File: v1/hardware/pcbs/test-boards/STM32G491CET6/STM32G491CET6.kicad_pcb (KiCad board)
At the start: 2 copper layers, 43 x 38 mm, 43 parts, among them J1 Conn_02x10_Odd_Even, J2 Conn_02x10_Odd_Even, J3 Conn_01x04, U1 STM32G491CETx, Y1 Crystal_GND24, Y2 Crystal

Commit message: not sure what i did
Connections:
- C6 pad 2: Net-(U1-VBAT) -> +3V3
- U1 pad 1: Net-(U1-VBAT) -> +3V3
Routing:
- net +3V3: track 35.4 -> 39.0 mm
- net Net-(U1-VBAT): track 3.65 -> 0.00 mm

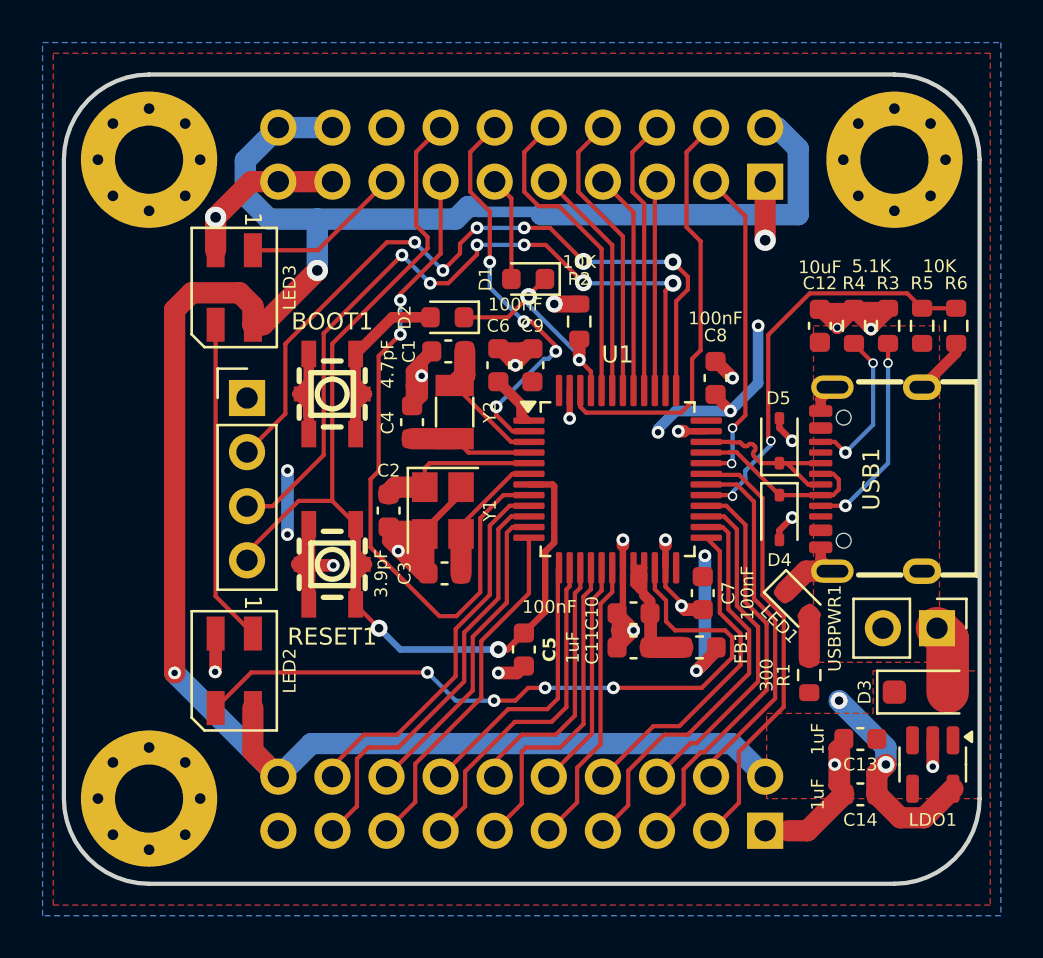
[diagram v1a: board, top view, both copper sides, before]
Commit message: fixed STM32G4 breakout board boot pin floating, and changed RGB LEDs to indicator LED
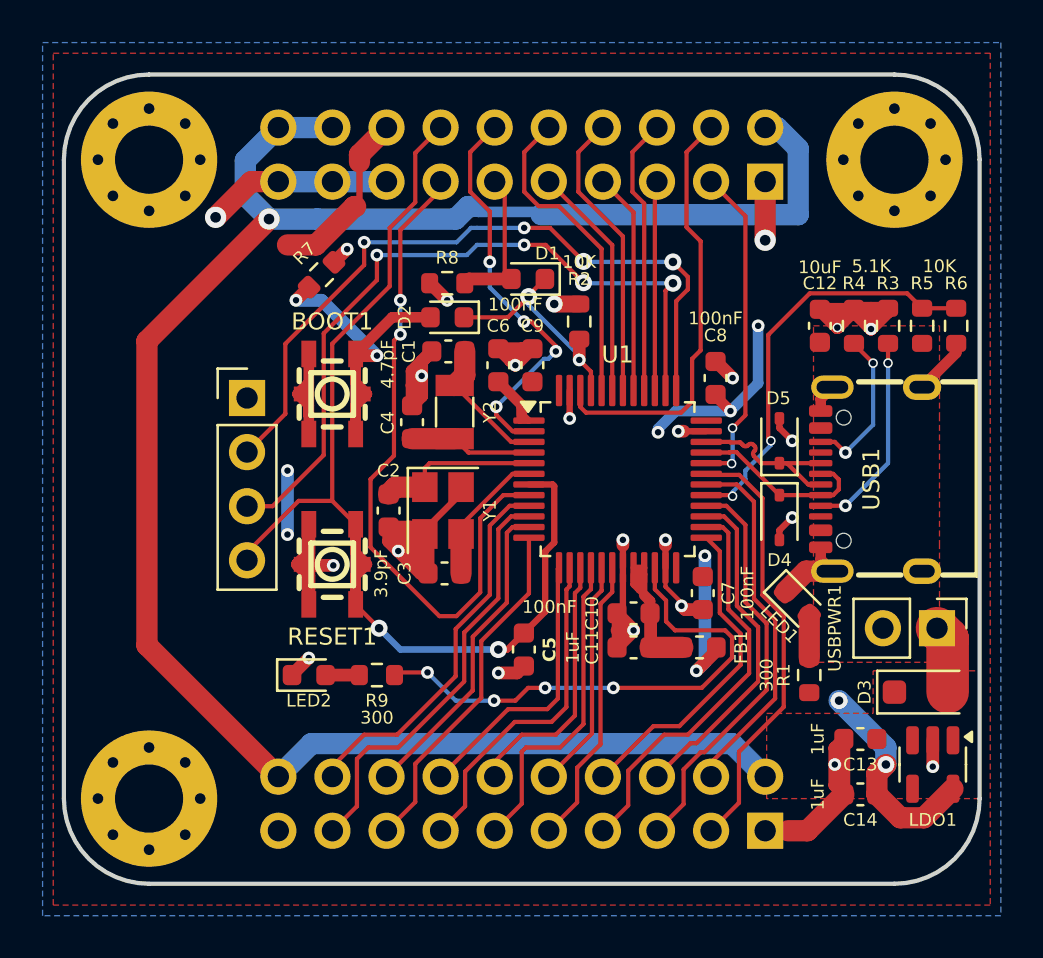
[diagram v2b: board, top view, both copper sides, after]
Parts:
- removed LED3: SK6812MINI, LED_SMD:LED_SK6812MINI_PLCC4_3.5x3.5mm_P1.75mm
- added R7: 10K, Resistor_SMD:R_0603_1608Metric, F.Cu at (-9.40, -9.60)
- added R8: 10K, Resistor_SMD:R_0603_1608Metric, F.Cu at (-3.50, -9.20)
- added R9: 300, Resistor_SMD:R_0603_1608Metric, F.Cu at (-6.80, 9.20)
- LED2: value SK6812MINI -> C965799; footprint LED_SMD:LED_SK6812MINI_PLCC4_3.5x3.5mm_P1.75mm -> LED_SMD:LED_0603_1608Metric
- moved LED2 3.51 mm to (-10.0, 9.20), turned to 0 degrees
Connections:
- J1 pad 15: /SK6812_data -> GND
- LED2 pad 1: Net-(LED2-DOUT) -> GND
- LED2 pad 2: GND -> Net-(LED2-A)
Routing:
- net Net-(LED2-DOUT): track 15.2 -> 0.00 mm
- net /PB10: track 33.4 -> 24.4 mm
- net +3V3: track 39.0 -> 47.3 mm
- net +5V: track 101.7 -> 93.5 mm, vias 2 -> 1
- net /SK6812_data: track 7.61 -> 0.00 mm
- net Net-(D2-A): track 12.2 -> 19.0 mm, vias 0 -> 2
- net GND: track 99.1 -> 101.5 mm, vias 22 -> 24
- net /BOOT0: track 4.89 -> 7.16 mm
- net Net-(LED2-A): track 0.00 -> 1.59 mm
- net /SWDIO: track 34.9 -> 34.1 mm, vias 6 -> 4
- net /SWCLK: track 35.7 -> 35.0 mm, vias 6 -> 4
